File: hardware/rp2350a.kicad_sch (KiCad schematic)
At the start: 34 parts, among them Q26 AP1606, U10 RP2354A, U24 FXMAR2104UMX, X1 12MHz

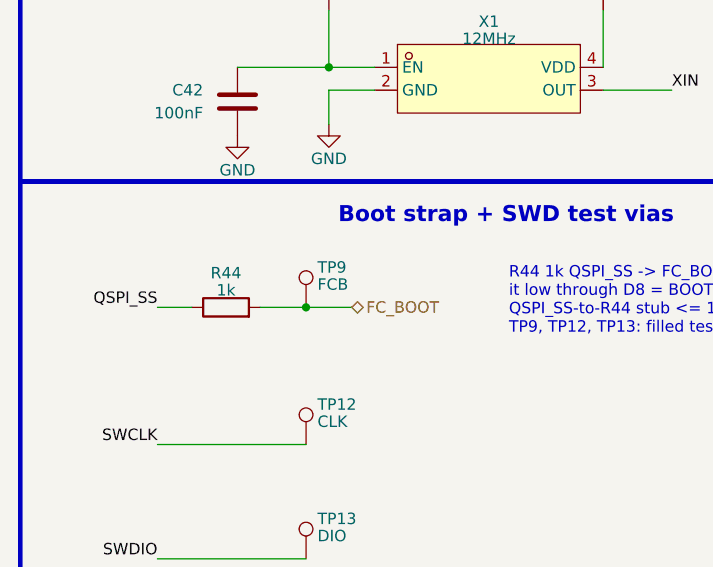
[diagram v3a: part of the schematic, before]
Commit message: Preserve owner ESC progress and allocate inner signal layers
Integrate the owner's retained placements and copper with the reviewed RP2354A mapping, restore both ESC bulk capacitors per channel, and carry the owner boot-testpoint deletion. Allocate In1/In4 for signals, In2 for continuous ground and In3 for power. Remove obsolete inner-layer routing restrictions and add native rule fixtures. This checkpoint precedes the new compact placement.

Validation: schematic parity zero; 28 GPIO mappings, 7 netlist checks and 32 rule fixtures pass. ERC has 12 existing warnings and no errors. The inherited board retains 269 DRC findings and 499 reported unconnected items. Layout is unfinished.
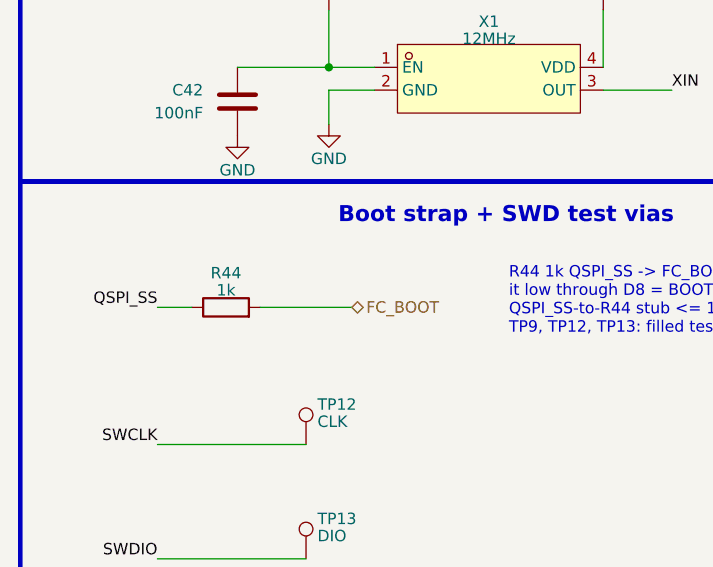
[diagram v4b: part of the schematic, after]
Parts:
- removed TP9: FCB, lib:TestPoint_Pad_D0.30mm_MicroVia_L, symbol Connector:TestPoint
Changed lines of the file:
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@@
 	)
 	(junction
-		(at 123.19 198.12)
-		(diameter 0)
-		(color 0 0 0 0)
-	)
-	(junction
 		(at 330.2 59.69)
 		(diameter 0)
@@
 	(wire
 		(pts
-			(xy 118.11 198.12) (xy 123.19 198.12)
-		)
-		(stroke
-			(width 0)
-			(type default)
-		)
-	)
-	(wire
-		(pts
 			(xy 388.62 189.23) (xy 396.24 189.23)
 		)
@@
 	(wire
 		(pts
-			(xy 123.19 198.12) (xy 128.27 198.12)
+			(xy 118.11 198.12) (xy 128.27 198.12)
 		)
 		(stroke
@@
 					(unit 1)
 				)
-			)
-		)
-	)
-	(symbol
-		(lib_id "Connector:TestPoint")
-		(at 123.19 198.12 0)
-		(unit 1)
-		(body_style 1)
-		(exclude_from_sim no)
-		(in_bom no)
-		(on_board yes)
-		(in_pos_files no)
-		(dnp no)
-		(property "Reference" "TP9"
-			(at 124.46 193.675 0)
-			(show_name no)
-			(do_not_autoplace no)
-			(effects
-				(font
-					(size 1.27 1.27)
-				)
-				(justify left)
-			)
-		)
-		(property "Value" "FCB"
-			(at 124.46 195.58 0)
-			(show_name no)
-			(do_not_autoplace no)
-			(effects
-				(font
-					(size 1.27 1.27)
-				)
-				(justify left)
-			)
-		)
-		(property "Footprint" "lib:TestPoint_Pad_D0.30mm_MicroVia_L"
-			(at 123.19 198.12 0)
-			(hide yes)
-			(show_name no)
-			(do_not_autoplace no)
-			(effects
-				(font
-					(size 1.27 1.27)
-				)
-			)
-		)
-		(property "Datasheet" ""
-			(at 123.19 198.12 0)
-			(hide yes)
-			(show_name no)
-			(do_not_autoplace no)
-			(effects
-				(font
-					(size 1.27 1.27)
-				)
-			)
-		)
-		(property "Description" "test point"
-			(at 123.19 198.12 0)
-			(hide yes)
-			(show_name no)
-			(do_not_autoplace no)
-			(effects
-				(font
-					(size 1.27 1.27)
-				)
-			)
-		)
-		(pin "1"
-		)
-		(instances
-			(project "OpenAIO-Whoop"
-				(path "/2c3a7206-1e66-4d43-a02f-491225e20dd6/df951d63-8e6a-5171-a7c4-15005f1245fb"
-					(reference "TP9")
-					(unit 1)
-				)
